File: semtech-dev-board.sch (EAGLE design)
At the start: 41 parts, among them Q2 BSS123, Q3 BSS84, U1 MIC5219 3.3V, X1 BU-SMA-G, X2 BU-SMA-G, X3 BU-SMA-G, X4 BU-SMA-G

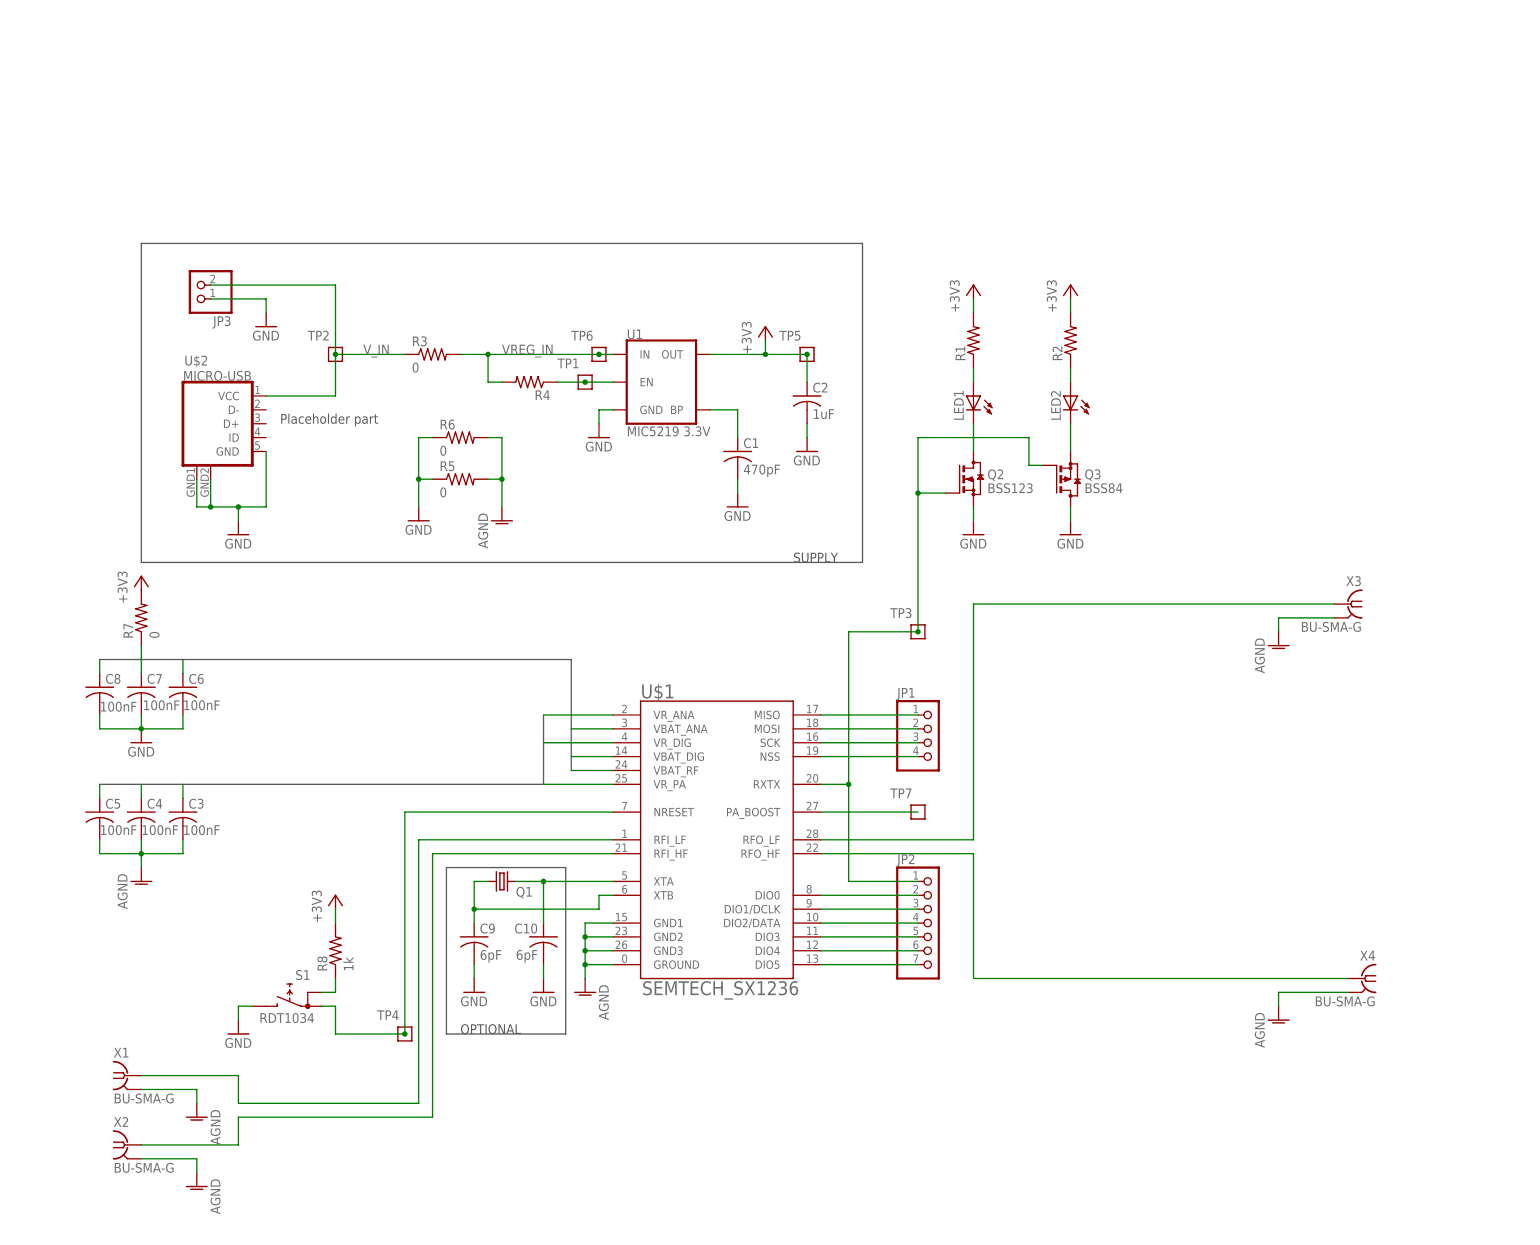
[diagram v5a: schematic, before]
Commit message: added biasing circuitry to match ref design for sx1233
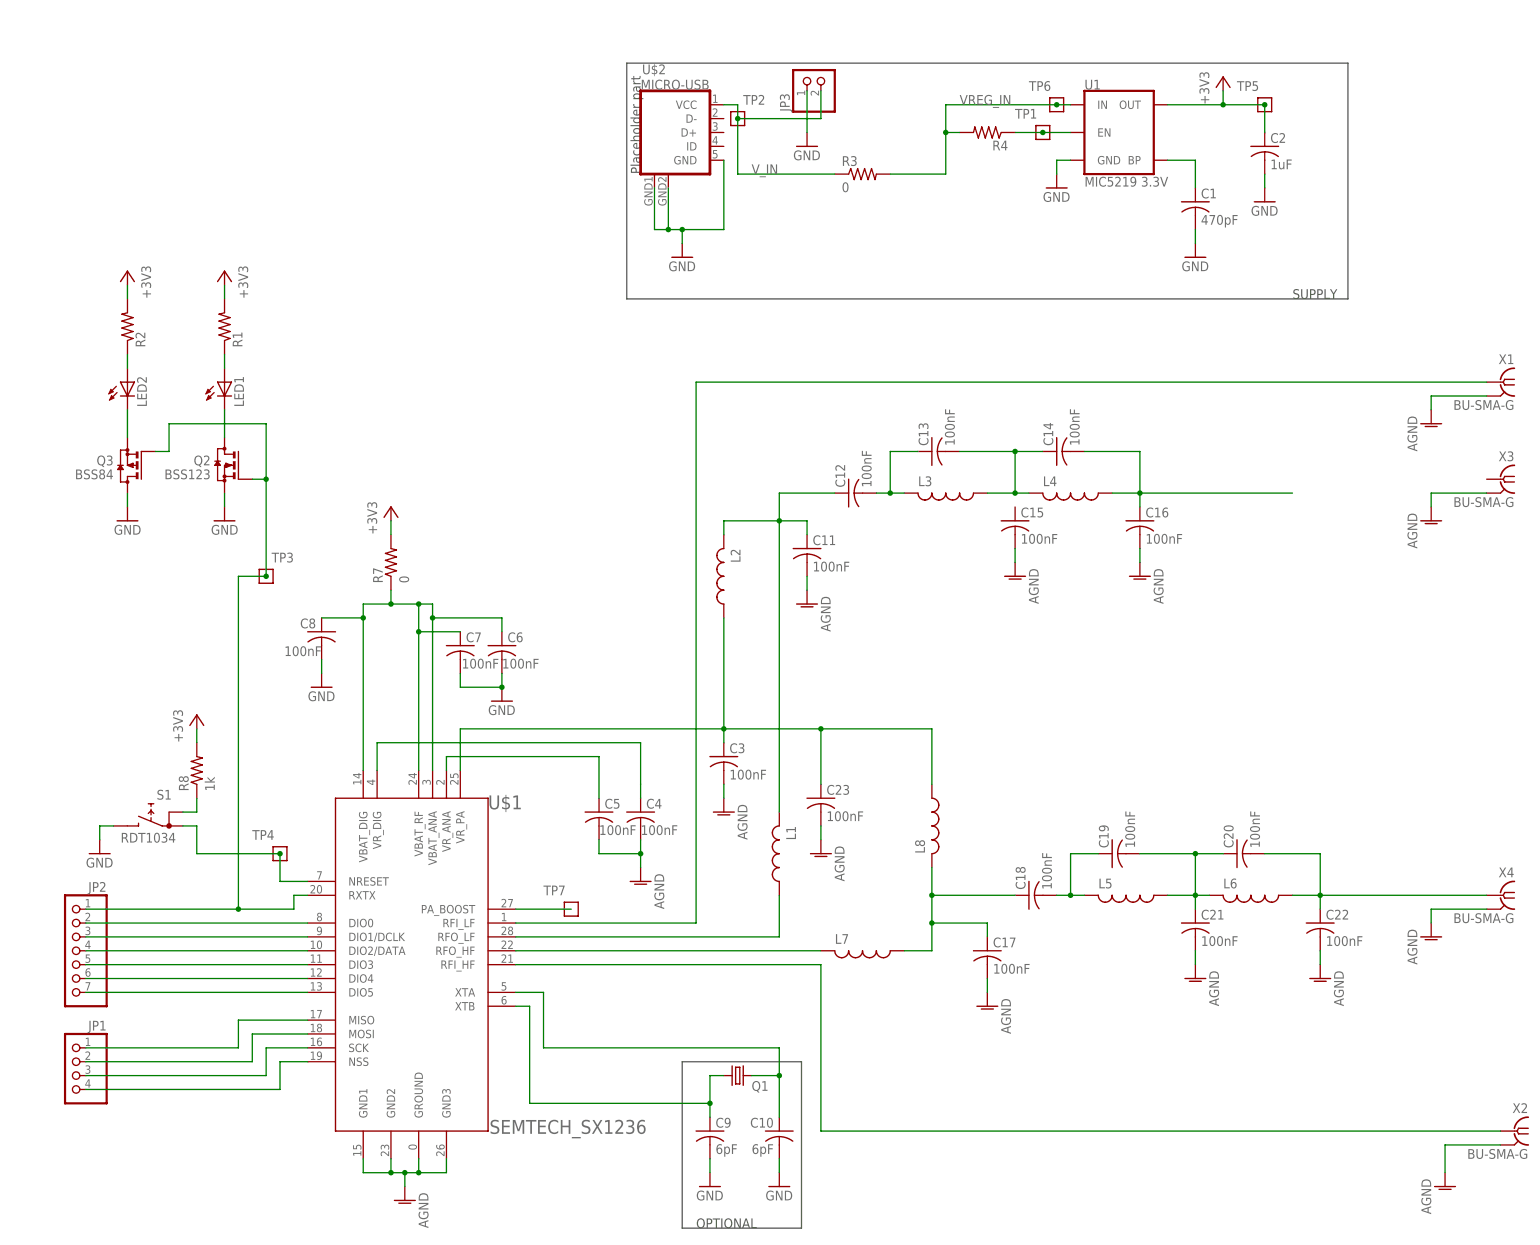
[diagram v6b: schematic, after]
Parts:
- removed R5, R6: 0, rcl:R-US_R0805
- added C11, C12, C13, C14, C15, C16, C17, C18, C19, C20, C21, C22, C23: 100nF, rcl:C-USC0805
- added L1, L2, L3, L4, L5, L6, L7, L8: (no value), rcl:L-USL3230M
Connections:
- removed net RFO_LF: U$1.RFO_LF, X3.1
- removed net VR_PA: C3.1, U$1.VR_PA
- new net N$14: C5.1, U$1.VR_ANA
- new net N$15: C23.1, C3.1, L2.1, L8.1, U$1.VR_PA
- new net N$16: L1.1, U$1.RFO_LF
- new net N$17: C11.1, C12.1, L1.2, L2.2
- new net N$18: L7.2, U$1.RFO_HF
- new net N$19: C17.1, C18.1, L7.1, L8.2
- new net N$22: C18.2, C19.1, L5.2
- new net N$23: C19.2, C20.1, C21.1, L5.1, L6.2
- new net N$26: C12.2, C13.1, L3.2
- new net N$27: C13.2, C14.1, L3.1, L4.2
- new net N$28: C14.2, C16.1, L4.1
- net +3V3: no longer U$1.VBAT_DIG, U$1.VBAT_RF
- net AGND: now also C11.2, C15.2, C16.2, C17.2, C21.2, C22.2, C23.2; no longer R5.2, R6.2
- net GND: no longer R5.1, R6.1
- net RFO_HF: now also C20.2, C22.1, L6.1; no longer U$1.RFO_HF
- net VBAT: now also U$1.VBAT_DIG, U$1.VBAT_RF
- net VR_ANA: now also U$1.VR_DIG; no longer C5.1, U$1.VR_ANA
- net VR_DIG: no longer U$1.VR_DIG
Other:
- moved on the sheet: C1, C10, C2, C3, C4, C5, C6, C7, C8, C9, JP1, JP2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

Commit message: formatted sch
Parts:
- added JP4: (no value), pinhead:PINHD-1X4
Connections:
- net N$16 renamed RFO_LF
- removed net N$18: L7.2, U$1.RFO_HF
- new net N$24: C3.1, JP4.1, L2.2
- new net VR_PA: JP4.2, JP4.3, U$1.VR_PA
- net GND: now also JP3.2; no longer JP3.1
- net N$15: now also JP4.4, L8.2; no longer C3.1, L2.1, L8.1, U$1.VR_PA
- net N$17: now also L2.1; no longer L2.2
- net N$19: now also L8.1; no longer L8.2
- net N$27: now also C15.1
- net N$28: now also X3.1
- net RFO_HF: now also L7.2, U$1.RFO_HF
- net V_IN: now also JP3.1; no longer JP3.2
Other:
- moved on the sheet: C1, C10, C11, C12, C13, C14, C15, C16, C17, C18, C19, C2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

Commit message: started 4 layer board
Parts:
- removed LED2: (no value), led:LEDCHIP-LED0805
- removed Q3: BSS84, transistor-small-signal:BSS84
- removed R7: 0, rcl:R-US_R0805
- removed R8: 1k, rcl:R-US_R0805
- removed TP3: TEST-POINT, low-gain-radio:TEST-POINT
- removed U$1: SEMTECH_SX1236, low-gain-radio:SEMTECH_SX1236
- removed U$2: MICRO-USB, microusb:MICRO-USB
- added JP5: (no value), pinhead:PINHD-1X2
- added R5: (no value), rcl:R-US_R0805
- added U2: (no value), microusb:USB""
- added U3: MIC5219 3.3V, SparkFun-IC-Power:V_REG_MIC52193.3V
- C1: value 470pF -> 100nF
- C10, C9: value 6pF -> 100nF
- C2: value 1uF -> 100nF
- C21: value 100nF -> 470pF
- C23: value 100nF -> 1uF
- C6, C7: value 100nF -> 6pF
- JP1: device pinhead:PINHD-1X4 -> pinhead:PINHD-1X7
- JP2: device pinhead:PINHD-1X7 -> pinhead:PINHD-1X4
- L5: device rcl:L-USL3230M -> rcl:L-USL1812
- Q1: value (none) -> BSS123; device crystal:CRYSTALSM49 -> transistor-small-signal:BSS123
- Q2: value BSS123 -> (none); device transistor-small-signal:BSS123 -> crystal:CRYSTALSM49
- R2: value (none) -> 1k; device rcl:R-US_M0805 -> rcl:R-US_R0805
- R4: value (none) -> 0
- U1: value MIC5219 3.3V -> SEMTECH_SX1236; device SparkFun-IC-Power:V_REG_MIC52193.3V -> low-gain-radio:SEMTECH_SX1236
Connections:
- removed net N$20: LED2.C, Q3.S
- removed net N$7: LED2.A, R2.1
- new net RFO_HF_OUT: C19.2, C22.1, L8.1, X3.1
- net +3V3: now also C23.1, R3.2, U3.OUT; no longer C2.1, R7.2, R8.2, U1.OUT
- net 5219_EN: now also R5.1, U3.EN; no longer R4.1, U1.EN
- net AGND: now also C10.2, C12.2, C18.2, C20.2, C8.2, C9.2, U1.GND1, U1.GND2, U1.GND3, U1.GROUND; no longer C11.2, C15.2, C17.2, C21.2, C23.2, C3.2, U$1.GND1, U$1.GND2, U$1.GND3, U$1.GROUND
- net BP: now also C21.1, U3.BP; no longer C1.1, U1.BP
- net GND: now also C21.2, C23.2, C3.2, JP5.2, Q1.S, U2.GND, U3.GND; no longer C10.2, C8.2, C9.2, Q2.S, Q3.D, U$2.GND, U$2.GND@1, U$2.GND@2, U1.GND
- net N$1: now also Q1.D; no longer Q2.D
- net N$10: now also JP1.4, U1.DIO2/DATA; no longer JP2.4, U$1.DIO2/DATA
- net N$11: now also JP1.5, U1.DIO3; no longer JP2.5, U$1.DIO3
- net N$12: now also JP1.6, U1.DIO4; no longer JP2.6, U$1.DIO4
- net N$13: now also JP1.7, U1.DIO5; no longer JP2.7, U$1.DIO5
- net N$14: now also C4.1, U1.VR_ANA; no longer C5.1, U$1.VR_ANA
- net N$15: now also C9.1, L2.2; no longer C23.1, L8.2
- net N$17: now also C10.1, L1.1, L3.2; no longer C12.1, L1.2, L2.1
- net N$19: now also C12.1, C13.1, L2.1, L4.1; no longer C17.1, C18.1, L7.1, L8.1
- net N$2: now also C7.1, Q2.2, U1.XTA; no longer C10.1, Q1.2, U$1.XTA
- net N$22: now also C13.2, C15.1, L6.2; no longer C18.2, C19.1, L5.2
- net N$23: now also C15.2, C18.1, C19.1, L6.1, L8.2; no longer C19.2, C20.1, C21.1, L5.1, L6.2
- net N$24: now also C8.1, L1.2; no longer C3.1, L2.2
- net N$26: now also C11.2, C14.1, L5.2; no longer C12.2, C13.1, L3.2
- net N$27: now also C14.2, C16.1, C17.1, L5.1, L7.2; no longer C13.2, C14.1, C15.1, L3.1, L4.2
- net N$28: now also C17.2, C20.1, L7.1, X2.1; no longer C14.2, C16.1, L4.1, X3.1
- net N$3: now also JP2.1, U1.MISO; no longer JP1.1, U$1.MISO
- net N$4: now also R2.1; no longer R8.1
- net N$5: now also JP1.2, U1.DIO0; no longer JP2.2, U$1.DIO0
- net N$9: now also JP1.3, U1.DIO1/DCLK; no longer JP2.3, U$1.DIO1/DCLK
- net PA_BOOST: now also U1.PA_BOOST; no longer U$1.PA_BOOST
- net RFI_HF: now also U1.RFI_HF, X4.1; no longer U$1.RFI_HF, X2.1
- net RFI_LF: now also U1.RFI_LF; no longer U$1.RFI_LF
- net RFO_HF: now also L4.2, U1.RFO_HF; no longer C20.2, C22.1, L6.1, L7.2, U$1.RFO_HF, X4.1
- net RFO_LF: now also L3.1, U1.RFO_LF; no longer L1.1, U$1.RFO_LF
- net RXTX: now also JP1.1, JP3.1, Q1.G, U1.RXTX; no longer JP2.1, Q2.G, Q3.G, TP3.1, U$1.RXTX
- net SPI_MOSI: now also JP2.2, U1.MOSI; no longer JP1.2, U$1.MOSI
- net SPI_NSS: now also JP2.4, U1.NSS; no longer JP1.4, U$1.NSS
- net SPI_SCK: now also JP2.3, U1.SCK; no longer JP1.3, U$1.SCK
- net SX1236_RST: now also U1.NRESET; no longer U$1.NRESET
- net VBAT: now also C1.1, C2.1, C3.1, R3.1, U1.VBAT_ANA, U1.VBAT_DIG, U1.VBAT_RF; no longer C6.1, C7.1, C8.1, R7.1, U$1.VBAT_ANA, U$1.VBAT_DIG, U$1.VBAT_RF
- net VREG_IN: now also R5.2, U3.IN; no longer R3.2, U1.IN
- net VR_ANA: now also U1.VR_DIG; no longer U$1.VR_DIG
- net VR_DIG: now also C5.1; no longer C4.1
- net VR_PA: now also U1.VR_PA; no longer U$1.VR_PA
- net V_IN: now also JP5.1, R4.1, U2.VBUS; no longer JP3.1, R3.1, U$2.VCC
- net XTALB: now also C6.1, Q2.1, U1.XTB; no longer C9.1, Q1.1, U$1.XTB
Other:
- note removed: "Placeholder part"
- moved on the sheet: C1, C10, C11, C12, C13, C14, C15, C16, C17, C18, C19, C2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
